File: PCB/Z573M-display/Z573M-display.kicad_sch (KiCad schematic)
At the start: 59 parts, among them J1 OSTVN02A150, J2 OSTVN02A150, J4 Conn_01x05_Socket, J5 Conn_01x06_Socket, Q1 MPSA92, Q10 MPSA42, Q11 MPSA42, Q12 MPSA42, Q13 MPSA42, Q2 MPSA92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

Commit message: Horizontal pins
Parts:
- J4: footprint nixie-2.1-footprints:PinHeader_1x05_P2.54mm_Vertical -> Connector_PinHeader_2.54mm:PinHeader_1x05_P2.54mm_Horizontal
- J5: footprint nixie-2.1-footprints:PinHeader_1x06_P2.54mm_Vertical -> Connector_PinHeader_2.54mm:PinHeader_1x06_P2.54mm_Horizontal
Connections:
- net A0: now also J4.5 (Pin_5); no longer J4.1 (Pin_1)
- net A1: now also J4.4 (Pin_4); no longer J4.2 (Pin_2)
- net A3: now also J4.2 (Pin_2); no longer J4.4 (Pin_4)
- net DP: now also J4.1 (Pin_1); no longer J4.5 (Pin_5)
- net digit_0: now also J5.6 (Pin_6); no longer J5.1 (Pin_1)
- net digit_1: now also J5.5 (Pin_5); no longer J5.2 (Pin_2)
- net digit_2: now also J5.4 (Pin_4); no longer J5.3 (Pin_3)
- net digit_3: now also J5.3 (Pin_3); no longer J5.4 (Pin_4)
- net digit_4: now also J5.2 (Pin_2); no longer J5.5 (Pin_5)
- net digit_5: now also J5.1 (Pin_1); no longer J5.6 (Pin_6)

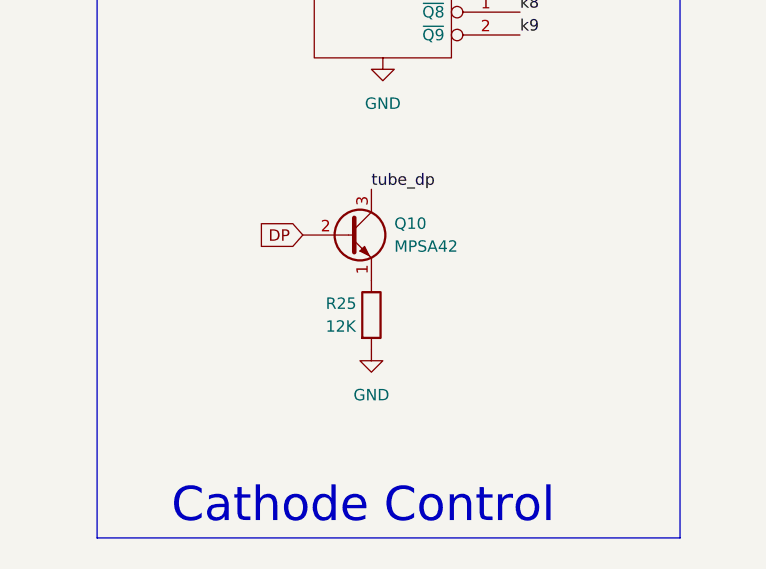
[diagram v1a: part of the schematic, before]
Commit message: Display and logic board edits
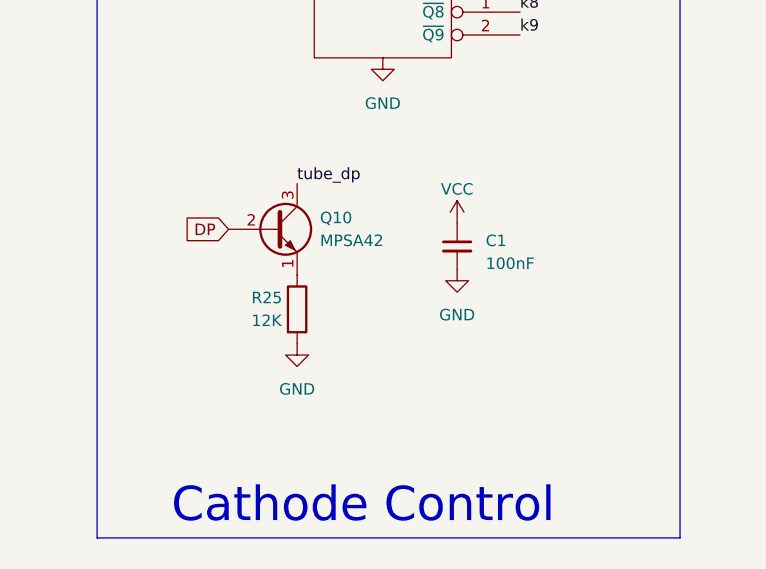
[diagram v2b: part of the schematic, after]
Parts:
- added C1: 100nF, Capacitor_THT:C_Disc_D4.7mm_W2.5mm_P5.00mm, symbol Device:C_Small
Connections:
- net GND: now also C1.2
- net VCC: now also C1.1
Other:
- moved on the sheet: Q10, R25
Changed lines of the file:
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@@
     (effects (font (size 1.27 1.27)) (justify right bottom))
   )
-  (label "tube_dp" (at 51.435 70.485 0) (fields_autoplaced)
+  (label "tube_dp" (at 43.18 69.85 0) (fields_autoplaced)
     (effects (font (size 1.27 1.27)) (justify left bottom))
   )
@@
     )
   )
-  (global_label "DP" (shape input) (at 43.815 75.565 180) (fields_autoplaced)
-    (effects (font (size 1.27 1.27)) (justify right))
-    (property "Intersheetrefs" "${INTERSHEET_REFS}" (at 38.8619 75.4856 0)
+  (global_label "DP" (shape input) (at 35.56 74.93 180) (fields_autoplaced)
+    (effects (font (size 1.27 1.27)) (justify right))
+    (property "Intersheetrefs" "${INTERSHEET_REFS}" (at 30.6069 74.8506 0)
       (effects (font (size 1.27 1.27)) (justify right) hide)
     )
@@
     )
   )
+  (symbol (lib_id "power:VCC") (at 60.96 74.295 0) (unit 1)
+    (in_bom yes) (on_board yes) (dnp no) (fields_autoplaced)
+    (property "Reference" "#PWR016" (at 60.96 78.105 0)
+      (effects (font (size 1.27 1.27)) hide)
+    )
+    (property "Value" "VCC" (at 60.96 70.485 0)
+      (effects (font (size 1.27 1.27)))
+    )
+    (property "Footprint" "" (at 60.96 74.295 0)
+      (effects (font (size 1.27 1.27)) hide)
+    )
+    (property "Datasheet" "" (at 60.96 74.295 0)
+      (effects (font (size 1.27 1.27)) hide)
+    )
+    (pin "1")
+    (instances
+      (project "Z573M-display"
+        (path "/a160f91f-03e0-4279-9371-b79f1f206693"
+          (reference "#PWR016") (unit 1)
+        )
+      )
+    )
+  )
   (symbol (lib_id "power:GND") (at 128.905 90.17 0) (unit 1)
     (in_bom yes) (on_board yes) (dnp no) (fields_autoplaced)
@@
     )
   )
-  (symbol (lib_id "power:GND") (at 51.435 88.265 0) (unit 1)
-    (in_bom yes) (on_board yes) (dnp no) (fields_autoplaced)
-    (property "Reference" "#PWR09" (at 51.435 94.615 0)
-      (effects (font (size 1.27 1.27)) hide)
-    )
-    (property "Value" "GND" (at 51.435 93.345 0)
+  (symbol (lib_id "power:GND") (at 43.18 87.63 0) (unit 1)
+    (in_bom yes) (on_board yes) (dnp no) (fields_autoplaced)
+    (property "Reference" "#PWR09" (at 43.18 93.98 0)
+      (effects (font (size 1.27 1.27)) hide)
+    )
+    (property "Value" "GND" (at 43.18 92.71 0)
       (effects (font (size 1.27 1.27)))
     )
-    (property "Footprint" "" (at 51.435 88.265 0)
-      (effects (font (size 1.27 1.27)) hide)
-    )
-    (property "Datasheet" "" (at 51.435 88.265 0)
+    (property "Footprint" "" (at 43.18 87.63 0)
+      (effects (font (size 1.27 1.27)) hide)
+    )
+    (property "Datasheet" "" (at 43.18 87.63 0)
       (effects (font (size 1.27 1.27)) hide)
     )
@@
         (path "/a160f91f-03e0-4279-9371-b79f1f206693"
           (reference "R26") (unit 1)
+        )
+      )
+    )
+  )
+  (symbol (lib_id "Device:C_Small") (at 60.96 76.835 0) (unit 1)
+    (in_bom yes) (on_board yes) (dnp no) (fields_autoplaced)
+    (property "Reference" "C1" (at 64.135 76.2063 0)
+      (effects (font (size 1.27 1.27)) (justify left))
+    )
+    (property "Value" "100nF" (at 64.135 78.7463 0)
+      (effects (font (size 1.27 1.27)) (justify left))
+    )
+    (property "Footprint" "Capacitor_THT:C_Disc_D4.7mm_W2.5mm_P5.00mm" (at 60.96 76.835 0)
+      (effects (font (size 1.27 1.27)) hide)
+    )
+    (property "Datasheet" "~" (at 60.96 76.835 0)
+      (effects (font (size 1.27 1.27)) hide)
+    )
+    (pin "1")
+    (pin "2")
+    (instances
+      (project "Z573M-display"
+        (path "/a160f91f-03e0-4279-9371-b79f1f206693"
+          (reference "C1") (unit 1)
         )
       )
@@
     )
   )
-  (symbol (lib_id "Device:R") (at 51.435 84.455 0) (unit 1)
-    (in_bom yes) (on_board yes) (dnp no)
-    (property "Reference" "R25" (at 46.355 83.185 0)
-      (effects (font (size 1.27 1.27)) (justify left))
-    )
-    (property "Value" "12K" (at 46.355 85.725 0)
-      (effects (font (size 1.27 1.27)) (justify left))
-    )
-    (property "Footprint" "Resistor_THT:R_Axial_DIN0207_L6.3mm_D2.5mm_P7.62mm_Horizontal" (at 49.657 84.455 90)
-      (effects (font (size 1.27 1.27)) hide)
-    )
-    (property "Datasheet" "~" (at 51.435 84.455 0)
+  (symbol (lib_id "power:GND") (at 60.96 79.375 0) (unit 1)
+    (in_bom yes) (on_board yes) (dnp no) (fields_autoplaced)
+    (property "Reference" "#PWR020" (at 60.96 85.725 0)
+      (effects (font (size 1.27 1.27)) hide)
+    )
+    (property "Value" "GND" (at 60.96 84.455 0)
+      (effects (font (size 1.27 1.27)))
+    )
+    (property "Footprint" "" (at 60.96 79.375 0)
+      (effects (font (size 1.27 1.27)) hide)
+    )
+    (property "Datasheet" "" (at 60.96 79.375 0)
+      (effects (font (size 1.27 1.27)) hide)
+    )
+    (pin "1")
+    (instances
+      (project "Z573M-display"
+        (path "/a160f91f-03e0-4279-9371-b79f1f206693"
+          (reference "#PWR020") (unit 1)
+        )
+      )
+    )
+  )
+  (symbol (lib_id "Device:R") (at 43.18 83.82 0) (unit 1)
+    (in_bom yes) (on_board yes) (dnp no)
+    (property "Reference" "R25" (at 38.1 82.55 0)
+      (effects (font (size 1.27 1.27)) (justify left))
+    )
+    (property "Value" "12K" (at 38.1 85.09 0)
+      (effects (font (size 1.27 1.27)) (justify left))
+    )
+    (property "Footprint" "Resistor_THT:R_Axial_DIN0207_L6.3mm_D2.5mm_P7.62mm_Horizontal" (at 41.402 83.82 90)
+      (effects (font (size 1.27 1.27)) hide)
+    )
+    (property "Datasheet" "~" (at 43.18 83.82 0)
       (effects (font (size 1.27 1.27)) hide)
     )
@@
     )
   )
-  (symbol (lib_id "nixie-tube-clock-2.1:MPSA42") (at 48.895 75.565 0) (unit 1)
-    (in_bom yes) (on_board yes) (dnp no) (fields_autoplaced)
-    (property "Reference" "Q10" (at 53.975 74.2949 0)
-      (effects (font (size 1.27 1.27)) (justify left))
-    )
-    (property "Value" "MPSA42" (at 53.975 76.8349 0)
-      (effects (font (size 1.27 1.27)) (justify left))
-    )
-    (property "Footprint" "Package_TO_SOT_THT:TO-92_HandSolder" (at 53.975 77.47 0)
+  (symbol (lib_id "nixie-tube-clock-2.1:MPSA42") (at 40.64 74.93 0) (unit 1)
+    (in_bom yes) (on_board yes) (dnp no) (fields_autoplaced)
+    (property "Reference" "Q10" (at 45.72 73.6599 0)
+      (effects (font (size 1.27 1.27)) (justify left))
+    )
+    (property "Value" "MPSA42" (at 45.72 76.1999 0)
+      (effects (font (size 1.27 1.27)) (justify left))
+    )
+    (property "Footprint" "Package_TO_SOT_THT:TO-92_HandSolder" (at 45.72 76.835 0)
       (effects (font (size 1.27 1.27) italic) (justify left) hide)
     )
-    (property "Datasheet" "http://www.onsemi.com/pub_link/Collateral/MPSA42-D.PDF" (at 48.895 75.565 0)
+    (property "Datasheet" "http://www.onsemi.com/pub_link/Collateral/MPSA42-D.PDF" (at 40.64 74.93 0)
       (effects (font (size 1.27 1.27)) (justify left) hide)
     )
